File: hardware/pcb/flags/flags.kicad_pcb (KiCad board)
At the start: 2 copper layers, 62.2 x 21.6 mm, 6 parts, among them J1 Bus, J2 Control, J3 Sync, J4 Power, J5 Conn_01x08_Male, J6 Conn_01x08_Male

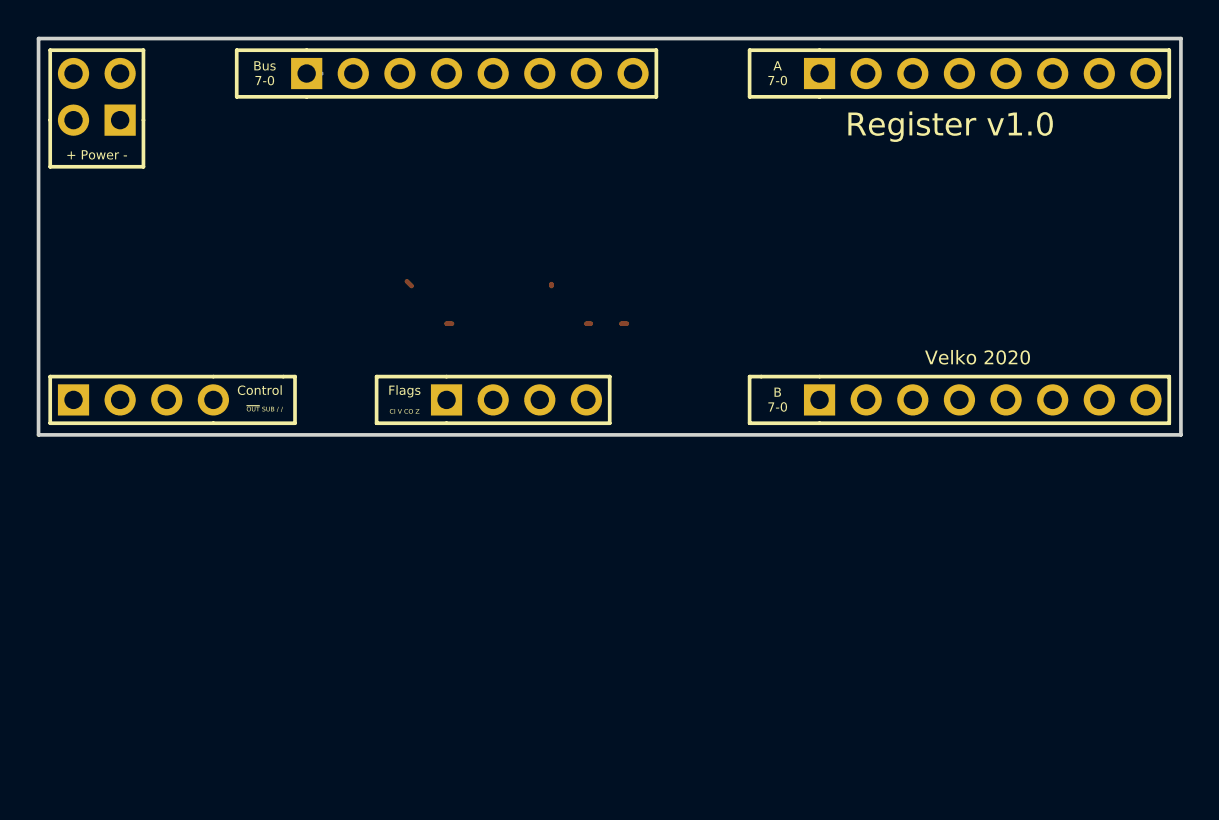
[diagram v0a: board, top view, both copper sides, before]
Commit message: Update connectors, export chips
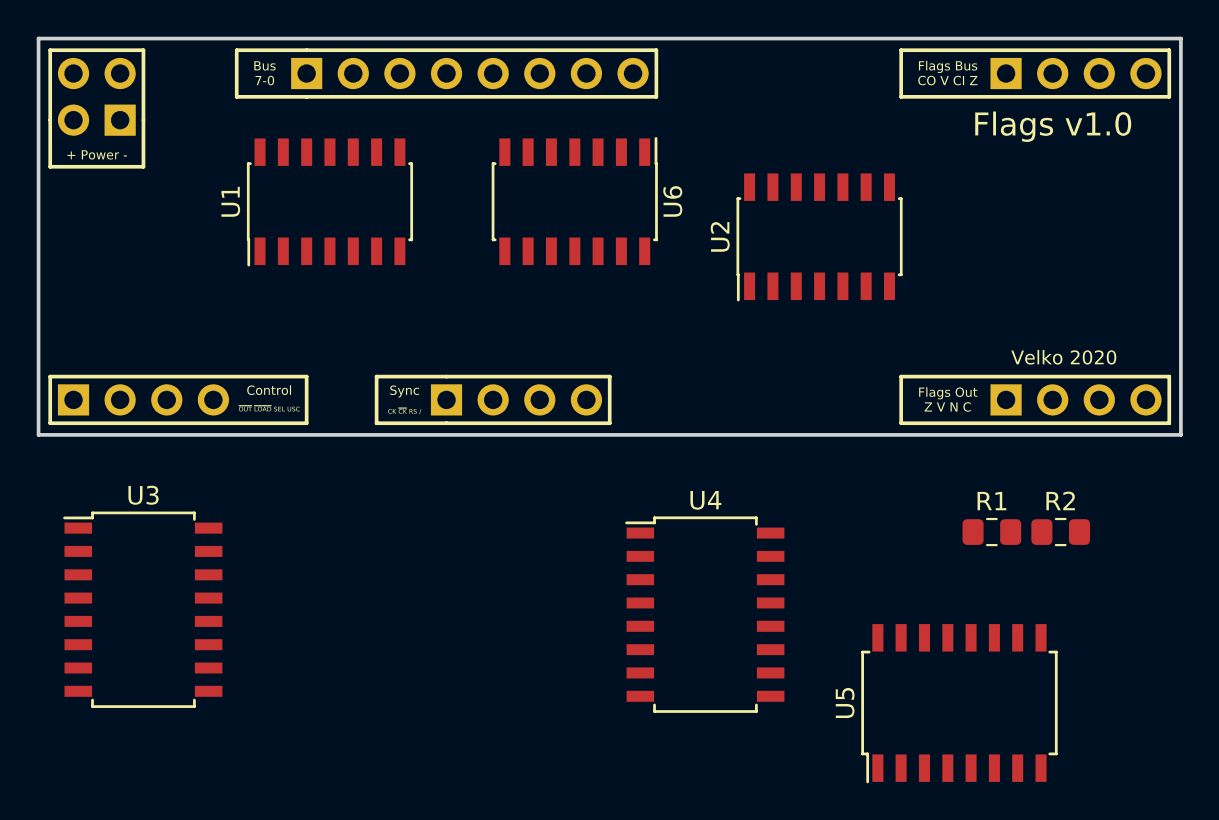
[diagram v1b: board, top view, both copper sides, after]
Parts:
- added R1: R, Resistor_SMD:R_0805_2012Metric_Pad1.15x1.40mm_HandSolder, F.Cu at (86.9, 63.1)
- added R2: R, Resistor_SMD:R_0805_2012Metric_Pad1.15x1.40mm_HandSolder, F.Cu at (90.6, 63.1)
- added U1: 74HC02, Package_SO:SOIC-14_3.9x8.7mm_P1.27mm, F.Cu at (50.8, 45.1)
- added U2: 74HC08, Package_SO:SOIC-14_3.9x8.7mm_P1.27mm, F.Cu at (77.5, 47.0)
- added U3: 74HC157, Package_SO:SOIC-16W_5.3x10.2mm_P1.27mm, F.Cu at (40.6, 67.3)
- added U4: 74HC173, Package_SO:SOIC-16W_5.3x10.2mm_P1.27mm, F.Cu at (71.3, 67.6)
- added U5: 74HC173, Package_SO:SOIC-16W_5.3x10.2mm_P1.27mm, F.Cu at (85.1, 72.4)
- added U6: 74HC125, Package_SO:SOIC-14_3.9x8.7mm_P1.27mm, F.Cu at (64.1, 45.1)
- J5: value Conn_01x08_Male -> Flags_Bus; footprint Connector_PinHeader_2.54mm:PinHeader_1x08_P2.54mm_Vertical -> Connector_PinHeader_2.54mm:PinHeader_1x04_P2.54mm_Vertical
- J6: value Conn_01x08_Male -> Ctrl_Out; footprint Connector_PinHeader_2.54mm:PinHeader_1x08_P2.54mm_Vertical -> Connector_PinHeader_2.54mm:PinHeader_1x04_P2.54mm_Vertical
- moved J5 10.2 mm to (87.6, 38.1)
- moved J6 10.2 mm to (87.6, 55.9)
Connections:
- J1 pad 1: Net-(J1-Pad1) -> BUS7
- J1 pad 2: Net-(J1-Pad2) -> BUS6
- J1 pad 3: Net-(J1-Pad3) -> BUS5
- J1 pad 4: Net-(J1-Pad4) -> BUS4
- J1 pad 5: Net-(J1-Pad5) -> BUS3
- J1 pad 6: Net-(J1-Pad6) -> BUS2
- J1 pad 7: Net-(J1-Pad7) -> BUS1
- J1 pad 8: Net-(J1-Pad8) -> BUS0
- J2 pad 1: Net-(J2-Pad1) -> ~OUT~
- J2 pad 2: Net-(J2-Pad2) -> ~LOAD~
- J2 pad 3: Net-(J2-Pad3) -> SEL
- J2 pad 4: Net-(J2-Pad4) -> USE_CARRY
- J3 pad 1: Net-(J3-Pad1) -> CLK
- J3 pad 2: Net-(J3-Pad2) -> ~CLK~
- J3 pad 3: Net-(J3-Pad3) -> RST
- J5 pad 1: Net-(J5-Pad1) -> CARRY_OUT
- J5 pad 2: Net-(J5-Pad2) -> OV_IN
- J5 pad 3: Net-(J5-Pad3) -> CARRY_IN
- J5 pad 4: Net-(J5-Pad4) -> Z_OUT
- J6 pad 1: Net-(J6-Pad1) -> Z_CTRL
- J6 pad 2: Net-(J6-Pad2) -> V_CTRL
- J6 pad 3: Net-(J6-Pad3) -> N_CTRL
- J6 pad 4: Net-(J6-Pad4) -> C_CTRL
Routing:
- net Net-(J1-Pad1): track 0.80 -> 0.00 mm
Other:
- board text added: "CK ~CK~ RS /"
- board text added: "Flags Bus CO V CI Z"
- board text added: "Flags Out Z V N C"
- board text added: "Flags v1.0"
- board text added: "Sync"
- board text added: "~OUT~ ~LOAD~ SEL USC"
- board text removed: "A 7-0"
- board text removed: "B 7-0"
- board text removed: "CI V CO Z"
- board text removed: "Flags"
- board text removed: "Register v1.0"
- board text removed: "~OUT~ SUB / /"

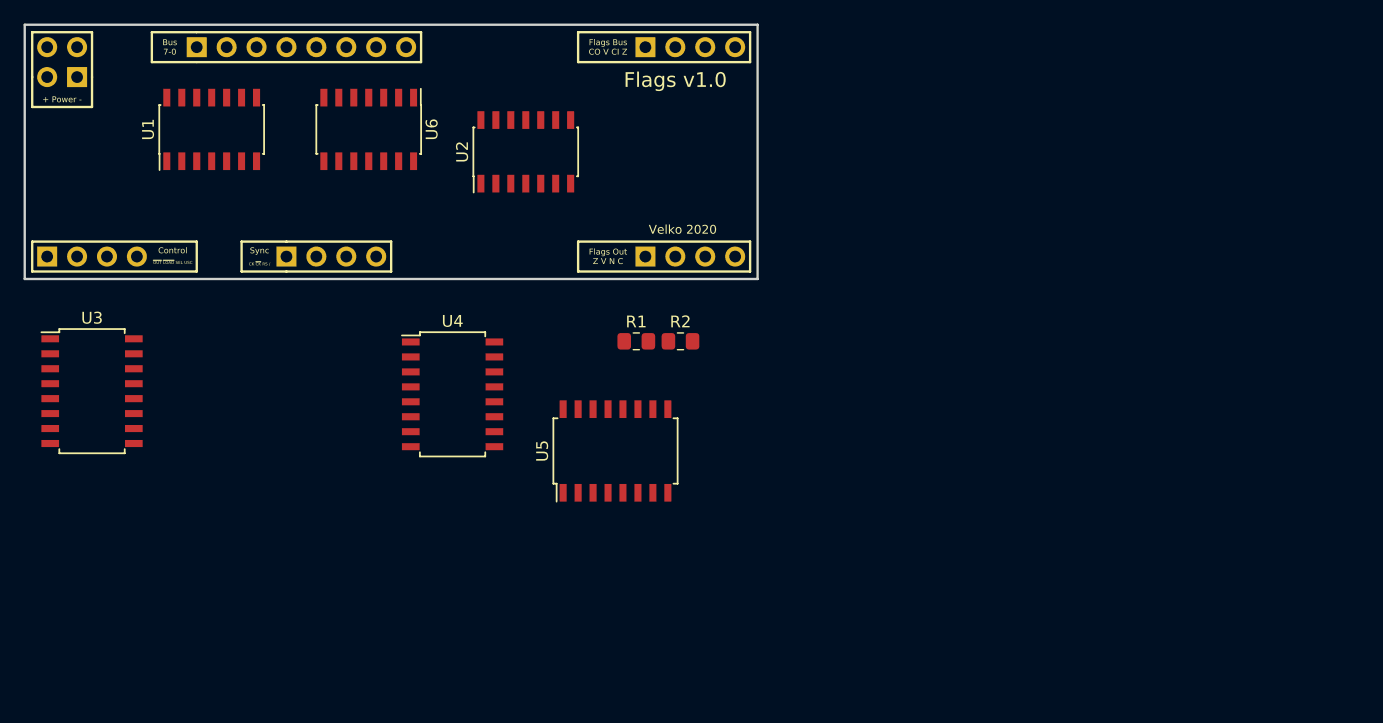
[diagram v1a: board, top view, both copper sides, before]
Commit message: Export parts to board
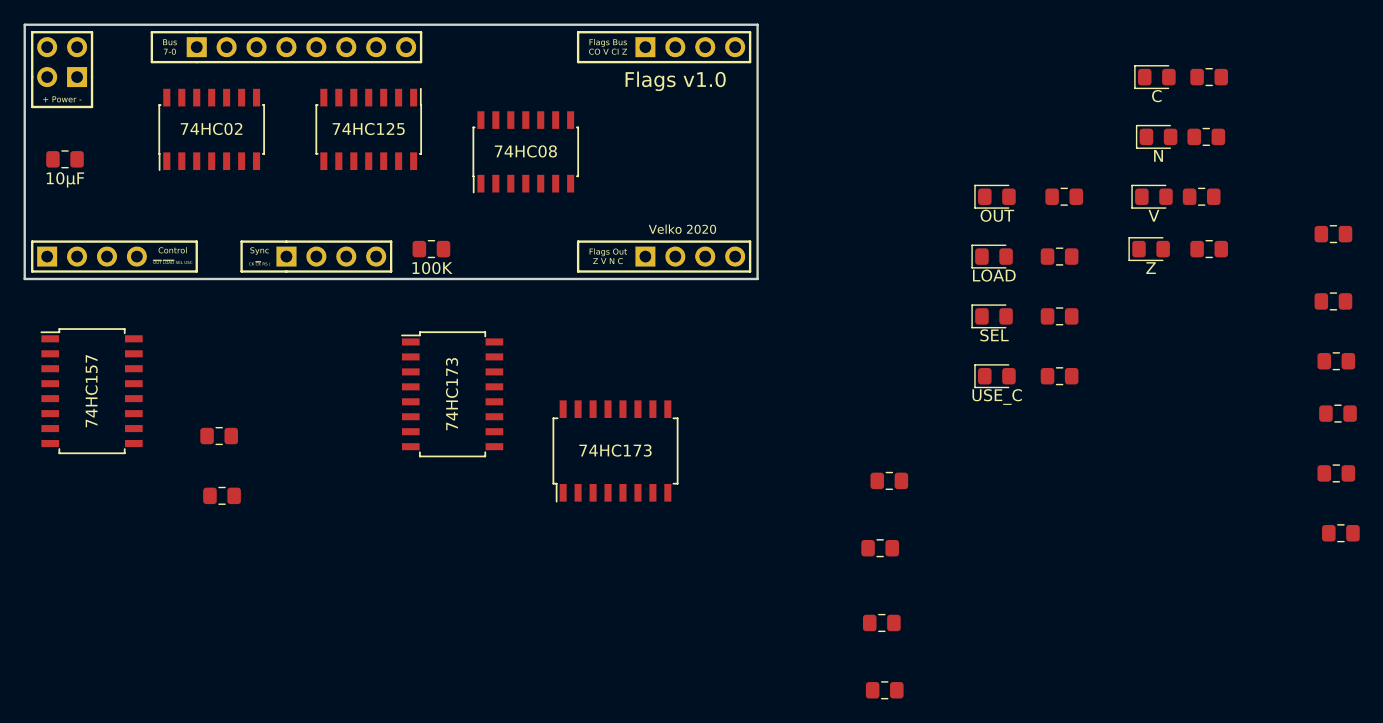
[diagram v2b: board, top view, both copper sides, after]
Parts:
- added C1: 100nF, Capacitor_SMD:C_0805_2012Metric_Pad1.15x1.40mm_HandSolder, F.Cu at (146.1, 54.0)
- added C2: 100nF, Capacitor_SMD:C_0805_2012Metric_Pad1.15x1.40mm_HandSolder, F.Cu at (146.1, 59.7)
- added C3: 100nF, Capacitor_SMD:C_0805_2012Metric_Pad1.15x1.40mm_HandSolder, F.Cu at (146.3, 64.8)
- added C4: 100nF, Capacitor_SMD:C_0805_2012Metric_Pad1.15x1.40mm_HandSolder, F.Cu at (146.4, 69.2)
- added C5: 100nF, Capacitor_SMD:C_0805_2012Metric_Pad1.15x1.40mm_HandSolder, F.Cu at (146.3, 74.3)
- added C6: 100nF, Capacitor_SMD:C_0805_2012Metric_Pad1.15x1.40mm_HandSolder, F.Cu at (146.7, 79.4)
- added C7: 10μF, Capacitor_SMD:C_0805_2012Metric_Pad1.15x1.40mm_HandSolder, F.Cu at (38.3, 47.6)
- added D1: Z, LED_SMD:LED_0805_2012Metric_Pad1.15x1.40mm_HandSolder, F.Cu at (130.6, 55.2)
- added D2: V, LED_SMD:LED_0805_2012Metric_Pad1.15x1.40mm_HandSolder, F.Cu at (130.8, 50.8)
- added D3: N, LED_SMD:LED_0805_2012Metric_Pad1.15x1.40mm_HandSolder, F.Cu at (131.2, 45.7)
- added D4: C, LED_SMD:LED_0805_2012Metric_Pad1.15x1.40mm_HandSolder, F.Cu at (131.1, 40.6)
- added D5: OUT, LED_SMD:LED_0805_2012Metric_Pad1.15x1.40mm_HandSolder, F.Cu at (117.5, 50.8)
- added D6: LOAD, LED_SMD:LED_0805_2012Metric_Pad1.15x1.40mm_HandSolder, F.Cu at (117.2, 55.9)
- added D7: SEL, LED_SMD:LED_0805_2012Metric_Pad1.15x1.40mm_HandSolder, F.Cu at (117.2, 61.0)
- added D8: USE_C, LED_SMD:LED_0805_2012Metric_Pad1.15x1.40mm_HandSolder, F.Cu at (117.5, 66.0)
- added R10: 330, Resistor_SMD:R_0805_2012Metric_Pad1.15x1.40mm_HandSolder, F.Cu at (122.8, 66.0)
- added R11: 10K, Resistor_SMD:R_0805_2012Metric_Pad1.15x1.40mm_HandSolder, F.Cu at (107.6, 80.6)
- added R12: 10K, Resistor_SMD:R_0805_2012Metric_Pad1.15x1.40mm_HandSolder, F.Cu at (107.7, 87.0)
- added R13: 10K, Resistor_SMD:R_0805_2012Metric_Pad1.15x1.40mm_HandSolder, F.Cu at (108.3, 74.9)
- added R14: 10K, Resistor_SMD:R_0805_2012Metric_Pad1.15x1.40mm_HandSolder, F.Cu at (108.0, 92.7)
- added R15: 100K, Resistor_SMD:R_0805_2012Metric_Pad1.15x1.40mm_HandSolder, F.Cu at (69.5, 55.2)
- added R3: 330, Resistor_SMD:R_0805_2012Metric_Pad1.15x1.40mm_HandSolder, F.Cu at (135.5, 55.2)
- added R4: 330, Resistor_SMD:R_0805_2012Metric_Pad1.15x1.40mm_HandSolder, F.Cu at (134.9, 50.8)
- added R5: 330, Resistor_SMD:R_0805_2012Metric_Pad1.15x1.40mm_HandSolder, F.Cu at (135.3, 45.7)
- added R6: 330, Resistor_SMD:R_0805_2012Metric_Pad1.15x1.40mm_HandSolder, F.Cu at (135.5, 40.6)
- added R7: 330, Resistor_SMD:R_0805_2012Metric_Pad1.15x1.40mm_HandSolder, F.Cu at (123.2, 50.8)
- added R8: 330, Resistor_SMD:R_0805_2012Metric_Pad1.15x1.40mm_HandSolder, F.Cu at (122.8, 55.9)
- added R9: 330, Resistor_SMD:R_0805_2012Metric_Pad1.15x1.40mm_HandSolder, F.Cu at (122.8, 61.0)
- R1, R2: value R -> 10K
- moved R2 40.0 mm to (51.4, 71.1)
- moved R1 37.5 mm to (51.7, 76.2)

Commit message: Preliminary placement
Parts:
- C1, C2, C7, R1, R10, R11, R12, R13, R14, R15, R2, R3, R4, R5, R6, R7, R8, R9, U1, U2: moved to B.Cu
- D5: value OUT -> BOUT
- D7: value SEL -> BIN
- D8: value USE_C -> USEC
- moved C3 95.0 mm to (54.3, 41.0), turned to 180 degrees
- moved C2 91.2 mm to (55.1, 52.7), turned to 180 degrees
- moved C4 82.5 mm to (65.9, 51.4), turned to 180 degrees
- moved R10 81.3 mm to (44.7, 43.3), turned to 180 degrees
- moved C5 80.5 mm to (70.4, 47.6), turned to 270 degrees
- moved R9 79.7 mm to (44.6, 45.5), turned to 180 degrees
- moved R8 79.5 mm to (44.7, 41.1)
- moved C1 78.9 mm to (67.2, 52.7), turned to 180 degrees
- moved R7 78.7 mm to (44.6, 47.6)
- moved D8 77.0 mm to (42.7, 47.9)
- moved R12 76.8 mm to (39.4, 52.0), turned to 270 degrees
- moved R11 76.3 mm to (36.8, 51.9), turned to 270 degrees
- moved R14 75.5 mm to (44.5, 51.9), turned to 270 degrees
- moved D7 75.4 mm to (42.7, 50.0)
- moved D6 75.3 mm to (42.7, 45.7)
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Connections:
- J6 pad 1: Z_CTRL -> V_CTRL
- J6 pad 2: V_CTRL -> C_CTRL
- J6 pad 3: N_CTRL -> Z_CTRL
- J6 pad 4: C_CTRL -> N_CTRL
- U1 pad 14: (no net) -> VCC
- U1 pad 2: BUS0 -> BUS3
- U1 pad 3: BUS1 -> BUS2
- U1 pad 5: BUS2 -> BUS1
- U1 pad 6: BUS3 -> BUS0
- U1 pad 7: (no net) -> GND
- U2 pad 1: Net-(U1-Pad1) -> Net-(U1-Pad4)
- U2 pad 14: (no net) -> VCC
- U2 pad 2: Net-(U1-Pad4) -> Net-(U1-Pad1)
- U2 pad 7: (no net) -> GND
- U6 pad 14: (no net) -> VCC
- U6 pad 7: (no net) -> GND
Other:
- board text added: "Flags Out V C Z N"
- board text removed: "Flags Out Z V N C"

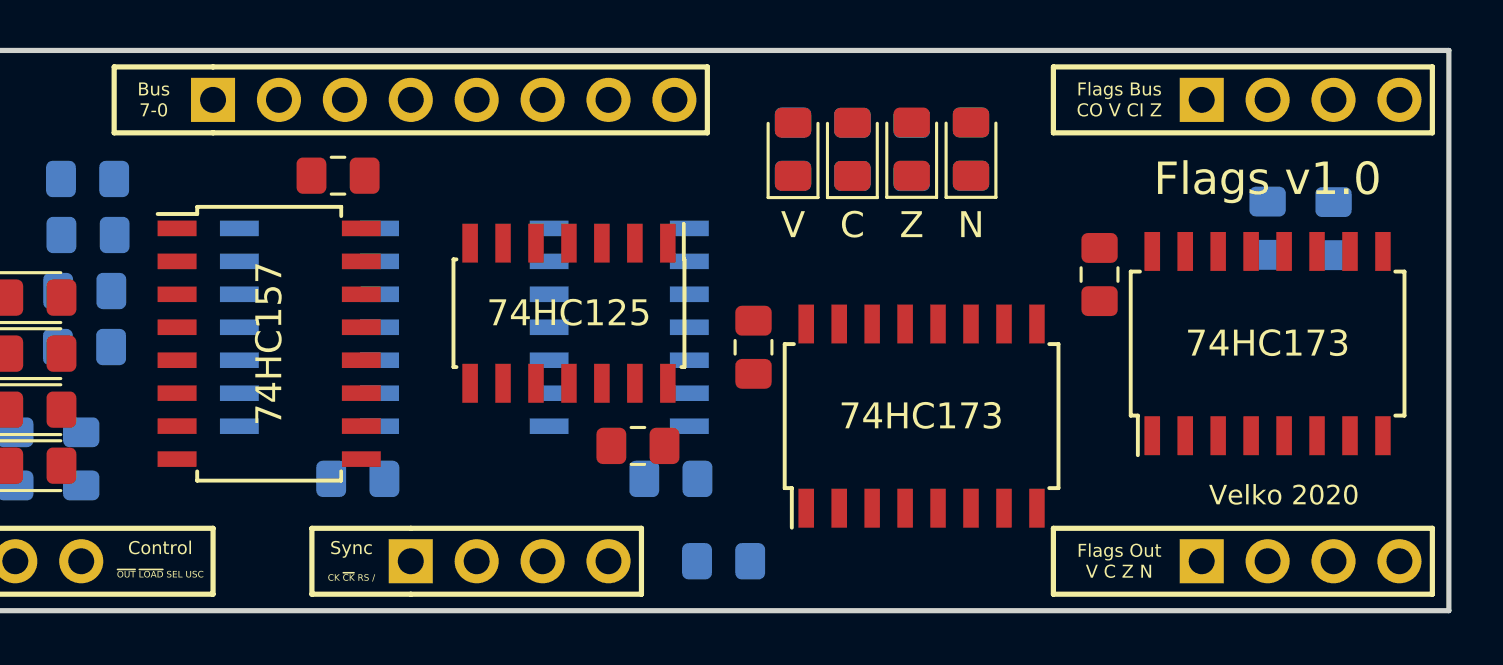
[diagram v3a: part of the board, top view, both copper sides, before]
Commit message: Swap gates for easier routing
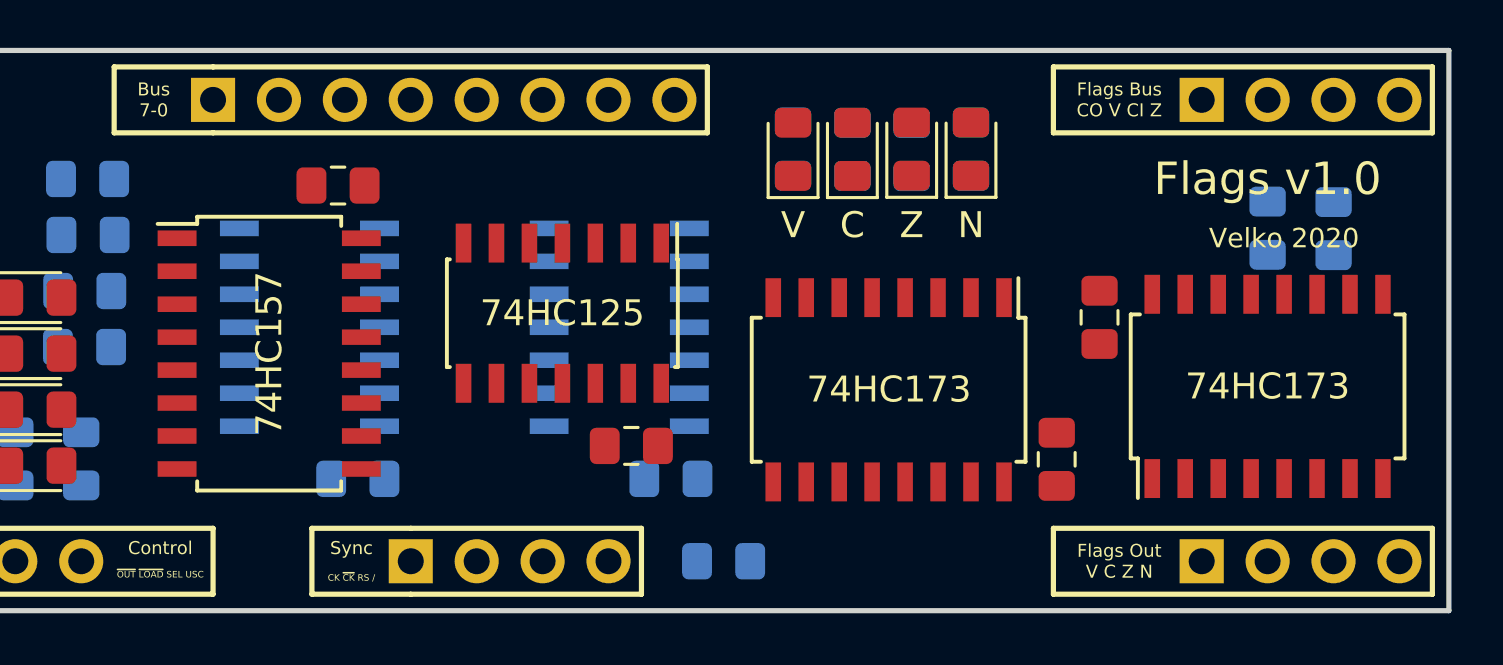
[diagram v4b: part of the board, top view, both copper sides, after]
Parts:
- C7: value 10μF -> 10uF
- moved C5 12.5 mm to (82.0, 52.0), turned to 90 degrees
- moved U5 1.65 mm to (90.2, 49.1)
- moved C6 1.65 mm to (83.7, 46.5)
- moved U4 1.63 mm to (75.6, 49.3), turned to 270 degrees
- moved C3 0.38 mm to (54.3, 41.4)
- moved U3 0.38 mm to (51.7, 47.9)
- moved U6 0.25 mm to (63.0, 46.3)
- moved C4 0.25 mm to (65.7, 51.4)
- turned R15 to 180 degrees
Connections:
- U1 pad 11: BUS6 -> BUS1
- U1 pad 12: BUS7 -> BUS0
- U1 pad 2: BUS3 -> BUS4
- U1 pad 3: BUS2 -> BUS5
- U1 pad 5: BUS1 -> BUS6
- U1 pad 6: BUS0 -> BUS7
- U1 pad 8: BUS4 -> BUS3
- U1 pad 9: BUS5 -> BUS2
- U2 pad 10: Net-(U2-Pad10) -> C_CTRL
- U2 pad 11: CARRY_OUT -> Z_OUT
- U2 pad 12: USE_CARRY -> Net-(U2-Pad12)
- U2 pad 13: N_CTRL -> Net-(U2-Pad13)
- U2 pad 3: Net-(U2-Pad3) -> Net-(U2-Pad13)
- U2 pad 4: Net-(U1-Pad10) -> Net-(U1-Pad13)
- U2 pad 5: Net-(U1-Pad13) -> Net-(U1-Pad10)
- U2 pad 6: Net-(U2-Pad10) -> Net-(U2-Pad12)
- U2 pad 8: Z_OUT -> CARRY_OUT
- U2 pad 9: Net-(U2-Pad3) -> USE_CARRY
- U5 pad 11: C_D -> N_D
- U5 pad 12: N_D -> Z_D
- U5 pad 13: V_D -> C_D
- U5 pad 14: Z_D -> V_D
- U5 pad 3: Z_CTRL -> V_CTRL
- U5 pad 4: V_CTRL -> C_CTRL
- U5 pad 5: N_CTRL -> Z_CTRL
- U5 pad 6: C_CTRL -> N_CTRL

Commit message: Reorder selector
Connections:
- net Net-(U3-Pad7) renamed V_I
- net Net-(U3-Pad9) renamed C_I
- U3 pad 12: Net-(U3-Pad12) -> Z_I
- U3 pad 13: BUS2 -> BUS0
- U3 pad 14: BUS7 -> Z_OUT
- U3 pad 2: Z_OUT -> BUS7
- U3 pad 3: BUS0 -> BUS2
- U3 pad 4: Net-(U3-Pad4) -> N_I
- U4 pad 12: Net-(U3-Pad12) -> N_I
- U4 pad 14: Net-(U3-Pad4) -> Z_I

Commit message: Move selector to back side (1st routable ver)
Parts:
- C3, U3: moved to B.Cu
- moved C3 28.7 mm to (83.0, 42.3)
- moved U3 28.7 mm to (80.4, 48.8)
- moved U6 8.13 mm to (54.9, 46.3)
- moved C4 6.16 mm to (60.5, 48.1), turned to 90 degrees
- moved C5 4.06 mm to (78.0, 52.0)
- moved U4 4.06 mm to (71.5, 49.3)
